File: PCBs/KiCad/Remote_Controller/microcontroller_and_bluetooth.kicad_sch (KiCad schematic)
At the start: 17 parts, among them J201 USB_C_Receptacle_USB2.0_16P, Q201 SS8050-G, Q202 SS8050-G, SW201 SW_Push, U201 USBLC6-2SC6, U202 ESP32-WROOM-32E, U203 CH340C

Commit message: Added new symbol fields and completed BOM
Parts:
- C201: JLCPCB Part # (none) -> C59461; Manufacturer Part # (none) -> CL10A226MQ8NRNC
- C202, C203, C206: JLCPCB Part # (none) -> C155422; Manufacturer Part # (none) -> CL05B104KA5NNNC
- C204: JLCPCB Part # (none) -> C14445; Manufacturer Part # (none) -> CL05A105KP5NNNC
- J201: JLCPCB Part # (none) -> C165948; Manufacturer Part # (none) -> TYPE-C-31-M-12
- Q201, Q202: JLCPCB Part # (none) -> C3199946; Manufacturer Part # (none) -> SS8050-G
- R201, R204, R205: JLCPCB Part # (none) -> C25531; Manufacturer Part # (none) -> 0402WGJ0103TCE
- R202, R203: JLCPCB Part # (none) -> C23186; Manufacturer Part # (none) -> 0603WAF5101T5E
- SW201: JLCPCB Part # (none) -> C2689642; Manufacturer Part # (none) -> PTS636SK25SMTRLFS
- U201: JLCPCB Part # (none) -> C7519; Manufacturer Part # (none) -> USBLC6-2SC6
- U202: JLCPCB Part # (none) -> C701341; Manufacturer Part # (none) -> ESP32-WROOM-32E-N4
- U203: JLCPCB Part # (none) -> C84681; Manufacturer Part # (none) -> CH340C

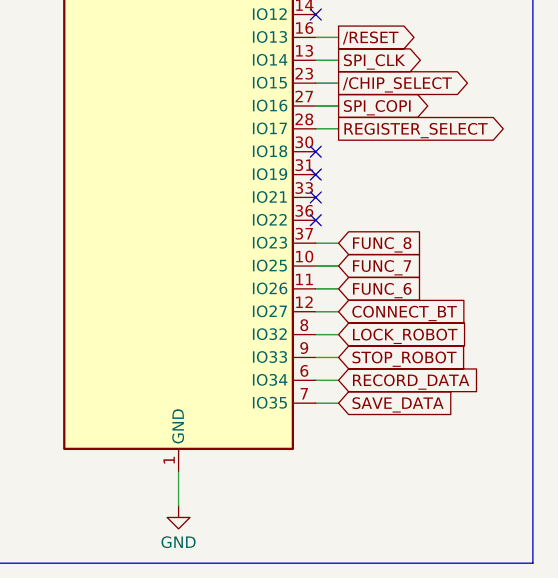
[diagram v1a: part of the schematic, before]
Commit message: Changed GPIO connections and completed tracing
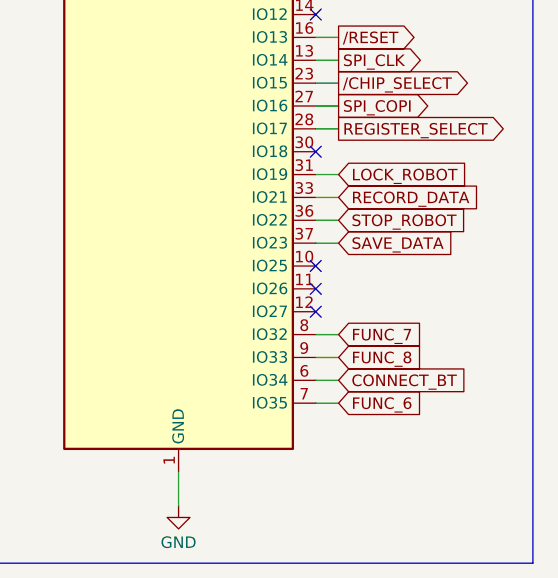
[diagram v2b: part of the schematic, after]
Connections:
- net CONNECT_BT: now also U202.6 (IO34); no longer U202.12 (IO27)
- net FUNC_6: now also U202.7 (IO35); no longer U202.11 (IO26)
- net FUNC_7: now also U202.8 (IO32); no longer U202.10 (IO25)
- net FUNC_8: now also U202.9 (IO33); no longer U202.37 (IO23)
- net LOCK_ROBOT: now also U202.31 (IO19); no longer U202.8 (IO32)
- net RECORD_DATA: now also U202.33 (IO21); no longer U202.6 (IO34)
- net SAVE_DATA: now also U202.37 (IO23); no longer U202.7 (IO35)
- net STOP_ROBOT: now also U202.36 (IO22); no longer U202.9 (IO33)

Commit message: Added differential USB signal
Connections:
- net D+: now also U201.6 (I/O1); no longer U201.4 (I/O2)
- net D-: now also U201.4 (I/O2); no longer U201.6 (I/O1)
- net D_RAW+: now also U201.1 (I/O1); no longer U201.3 (I/O2)
- net D_RAW-: now also U201.3 (I/O2); no longer U201.1 (I/O1)
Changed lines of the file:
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@@
 		)
 	)
-	(label "D_RAW+"
+	(label "D_RAW-"
 		(at 97.79 95.25 0)
 		(fields_autoplaced yes)
@@
 		)
 	)
-	(label "D_RAW-"
+	(label "D_RAW+"
 		(at 97.79 92.71 0)
 		(fields_autoplaced yes)
@@
 		)
 	)
-	(label "D+"
+	(label "D-"
 		(at 120.65 95.25 180)
 		(fields_autoplaced yes)
@@
 		)
 	)
-	(label "D-"
+	(label "D+"
 		(at 120.65 92.71 180)
 		(fields_autoplaced yes)

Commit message: Added silkscreen text and made manufacturing files
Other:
- title: (none) -> SurvBot - Remote Controller
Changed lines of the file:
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@@
 	(generator_version "8.0")
 	(paper "A4")
+	(title_block
+		(title "SurvBot - Remote Controller")
+		(date "2025-03-17")
+		(rev "1.0.0.")
+	)
 	(junction
 		(at 207.01 49.53)
